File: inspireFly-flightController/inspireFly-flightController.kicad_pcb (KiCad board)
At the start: 2 copper layers, 87 x 80 mm, 23 parts, among them J1 FTSH-107-01-L-DV-K-A, SW1 SW_Push, SW3 SW_Push, U1 STM32U595VITx, Y1 ABS07-32.768KHZ-T

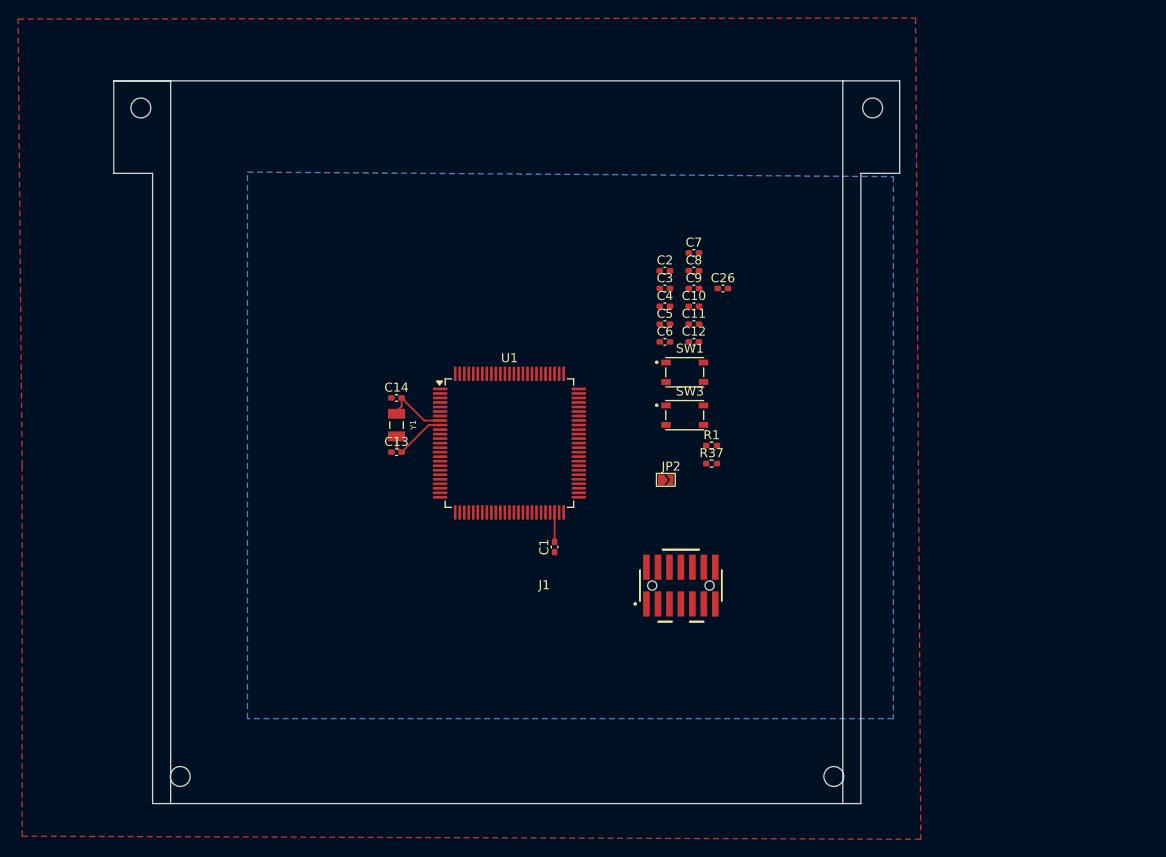
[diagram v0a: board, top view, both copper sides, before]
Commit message: Board sizes + Layer stackup
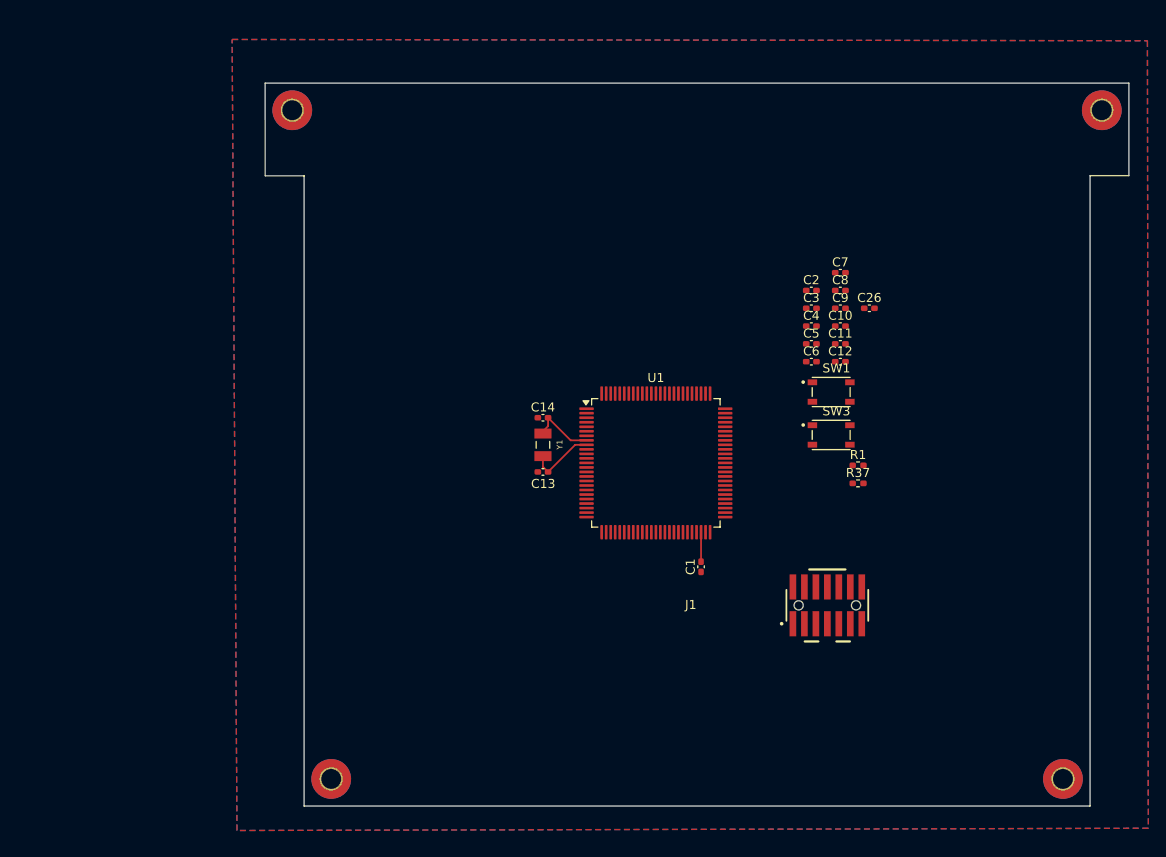
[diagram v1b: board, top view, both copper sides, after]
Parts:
- removed JP2: GND_DETECT, inspirefly:SmallJumper
- added H1: MountingHole_Pad, MountingHole:MountingHole_2.2mm_M2_Pad_TopBottom, F.Cu at (83.5, 42.1)
- added H2: MountingHole_Pad, MountingHole:MountingHole_2.2mm_M2_Pad_TopBottom, F.Cu at (173.1, 42.1)
- added H3: MountingHole_Pad, MountingHole:MountingHole_2.2mm_M2_Pad_TopBottom, F.Cu at (87.8, 116.2)
- added H4: MountingHole_Pad, MountingHole:MountingHole_2.2mm_M2_Pad_TopBottom, F.Cu at (168.8, 116.2)
- U1: value STM32U595VITx -> STM32U595VJT6
- moved C1 16.4 mm to (128.7, 92.7)
- moved C26 16.4 mm to (147.3, 64.1)
- moved R1 16.4 mm to (146.1, 81.5)
- moved R37 16.4 mm to (146.1, 83.5)
- moved SW1 16.4 mm to (143.1, 73.3)
- moved SW3 16.4 mm to (143.1, 78.1)
- moved C10 16.4 mm to (144.1, 66.0)
- moved C3 16.4 mm to (140.9, 64.1)
- moved C4 16.4 mm to (140.9, 66.0)
- moved C9 16.4 mm to (144.1, 64.1)
- moved C11 16.4 mm to (144.1, 68.0)
- moved C12 16.4 mm to (144.1, 70.0)
- moved C13 16.4 mm to (111.2, 82.2)
- moved C14 16.4 mm to (111.2, 76.2)
- moved C2 16.4 mm to (140.9, 62.1)
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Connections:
- J1 pad 11: Net-(JP2-B) -> GND
- U1 pad 15: unconnected-(U1-PC0-Pad15) -> DEBUG_LPUART_RX
- U1 pad 16: unconnected-(U1-PC1-Pad16) -> DEBUG_LPUART_TX
- U1 pad 47: DEBUG_LPUART_RX -> unconnected-(U1-PB10-Pad47)
- U1 pad 51: DEBUG_LPUART_TX -> unconnected-(U1-PB12-Pad51)
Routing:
- added copper zone on In2.Cu, net +3.3V
- added copper zone on In1.Cu, net GND
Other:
- board size 87 x 80 mm -> 95.6 x 80 mm
- copper layers 2 -> 4

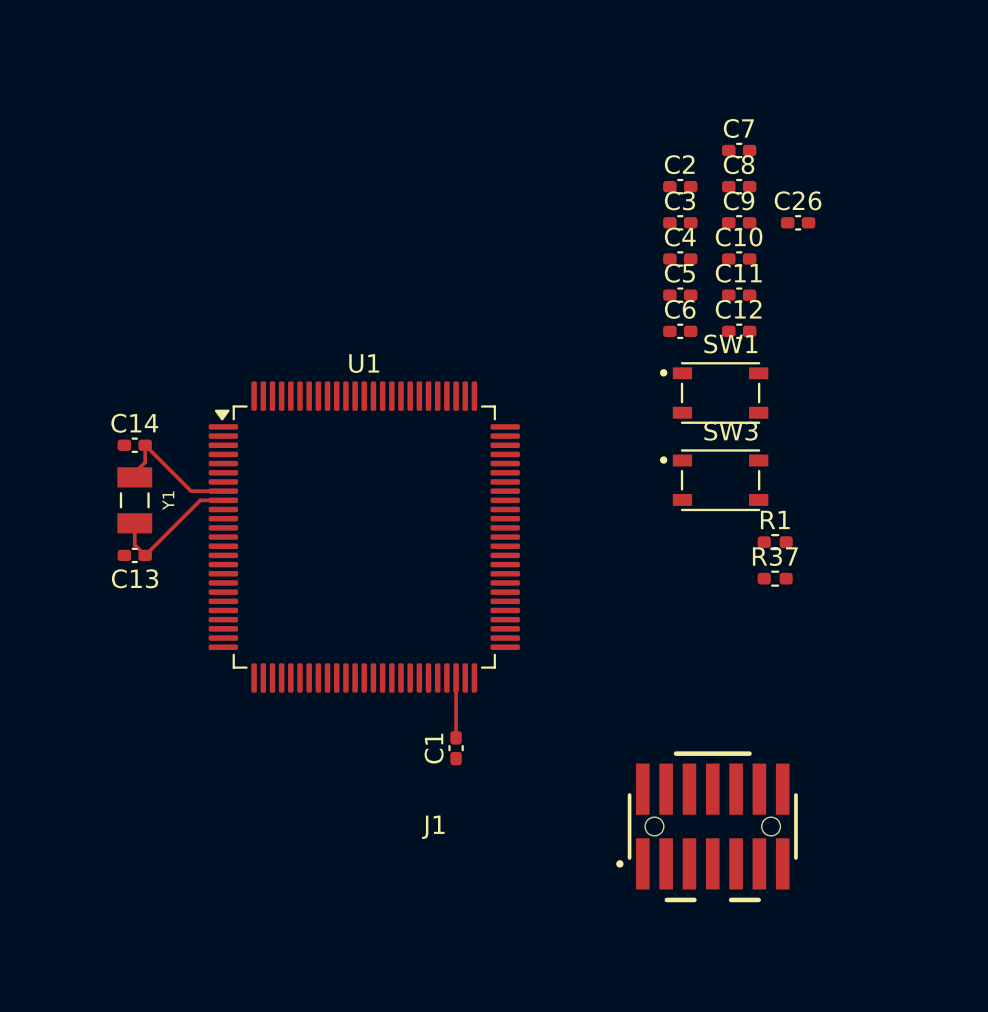
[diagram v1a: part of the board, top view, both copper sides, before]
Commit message: continued routing caps + updated footprints
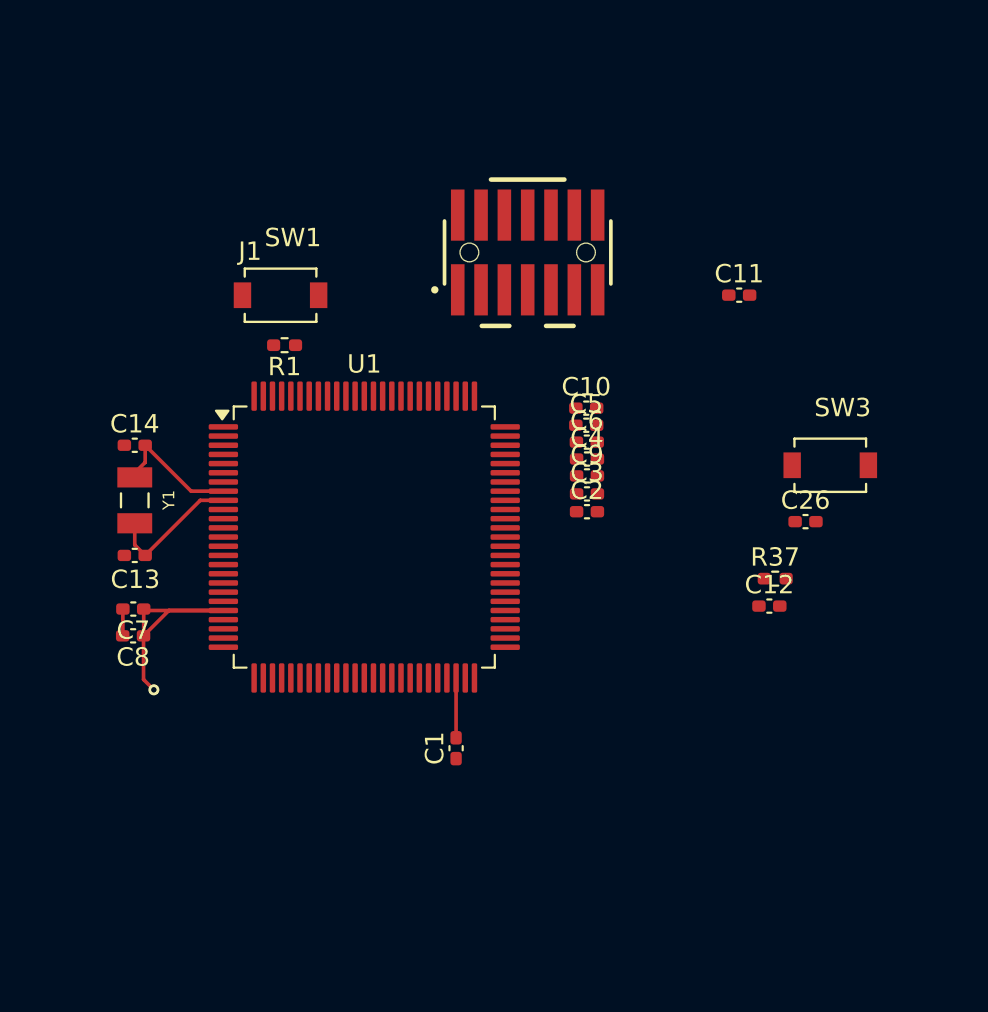
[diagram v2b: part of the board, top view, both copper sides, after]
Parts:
- SW1, SW3: footprint inspireFly-EPS-footprints:SW_PTS810_SJM_250_SMTR_LFS -> inspirefly:SW_TL1015AF160QG
- moved C7 41.4 mm to (111.1, 85.1), turned to 180 degrees
- moved C8 41.1 mm to (111.1, 86.6), turned to 180 degrees
- moved J1 32.8 mm to (132.6, 65.7)
- moved R1 28.8 mm to (119.4, 70.7), turned to 180 degrees
- moved SW1 24.5 mm to (119.2, 68.0)
- moved C2 18.4 mm to (135.8, 79.8)
- moved C26 16.3 mm to (147.7, 80.3)
- moved C9 16.1 mm to (135.8, 77.9)
- moved C3 15.6 mm to (135.8, 78.8)
- moved C12 15.1 mm to (145.8, 85.0)
- moved C4 12.0 mm to (135.8, 76.9)
- moved C10 11.6 mm to (135.8, 74.2)
- moved C5 8.74 mm to (135.8, 75.1)
- moved C6 7.89 mm to (135.8, 76.0)
- moved SW3 6.03 mm to (149.1, 77.3)
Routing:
- net +3.3V: track 0.00 -> 13.9 mm, vias 0 -> 1
- net GND: track 0.00 -> 1.46 mm

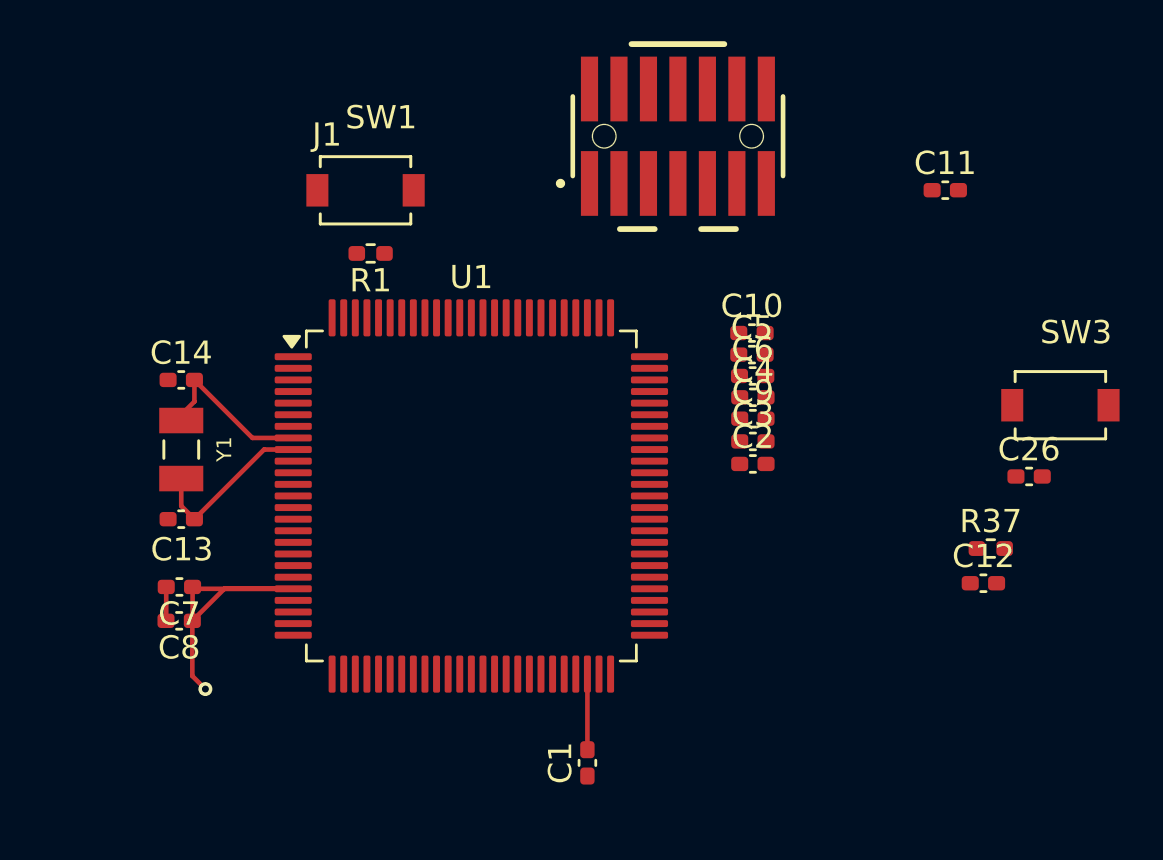
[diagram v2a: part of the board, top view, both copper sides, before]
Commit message: routed all power cap
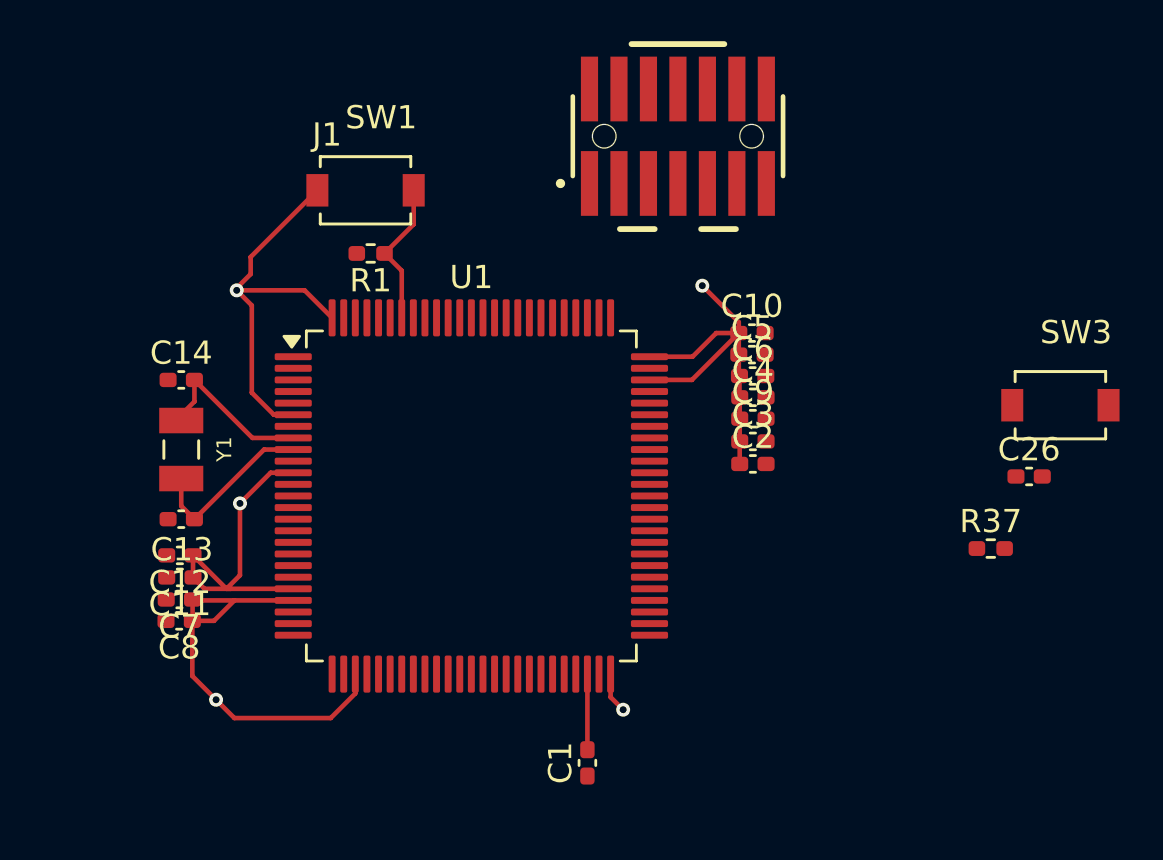
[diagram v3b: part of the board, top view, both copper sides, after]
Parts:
- moved C11 37.0 mm to (111.2, 84.7), turned to 180 degrees
- moved C12 34.6 mm to (111.2, 83.8), turned to 180 degrees
- moved C7 0.54 mm to (111.1, 85.7)
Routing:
- net +3.3V: track 13.9 -> 69.6 mm, vias 1 -> 5
- net Net-(U1-PH3-BOOT0): track 0.00 -> 6.32 mm
- net GND: track 1.46 -> 0.01 mm

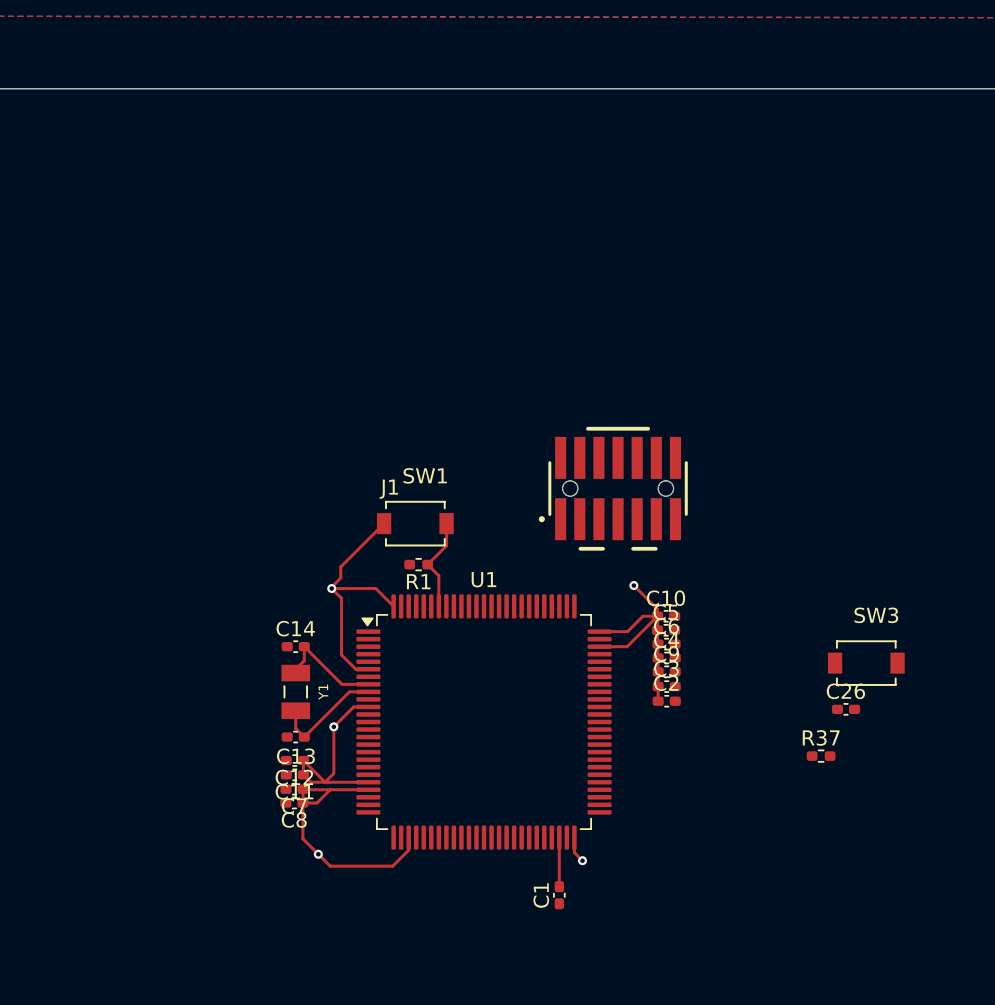
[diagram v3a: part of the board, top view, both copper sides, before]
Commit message: rerouted power caps +stlink
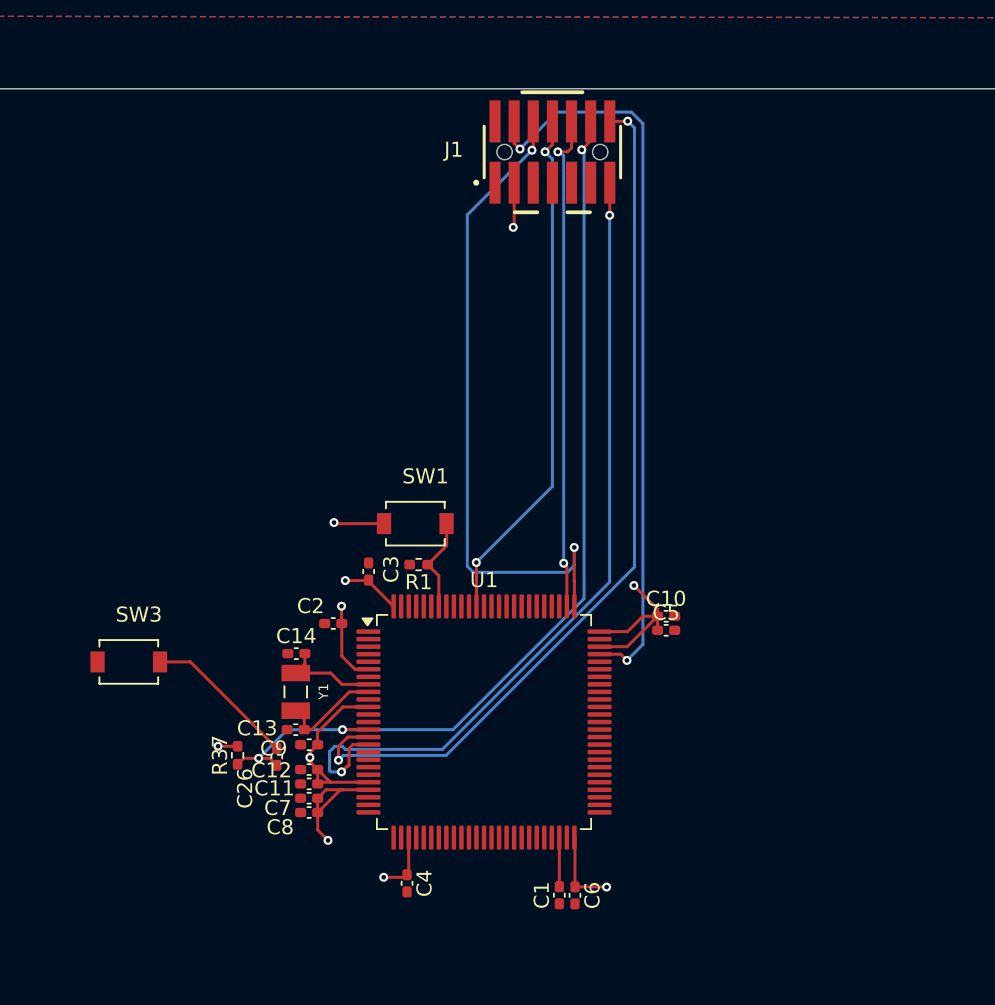
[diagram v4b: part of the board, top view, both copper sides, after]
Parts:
- moved SW3 49.0 mm to (100.1, 77.2)
- moved R37 38.7 mm to (107.3, 83.4), turned to 90 degrees
- moved C26 37.9 mm to (110.0, 83.5), turned to -90 degrees
- moved C9 24.2 mm to (112.1, 82.7), turned to 180 degrees
- moved C4 22.8 mm to (118.6, 91.9), turned to -90 degrees
- moved J1 22.8 mm to (128.2, 43.4)
- moved C2 22.7 mm to (113.7, 74.7), turned to 180 degrees
- moved C3 21.2 mm to (116.0, 71.2), turned to 90 degrees
- moved C6 17.8 mm to (129.8, 92.7), turned to -90 degrees
- moved C8 1.17 mm to (112.1, 87.2)
- moved C7 1.14 mm to (112.1, 86.2)
- moved C11 1.12 mm to (112.1, 85.3)
- moved C12 1.12 mm to (112.1, 84.3)
- moved C13 0.49 mm to (111.2, 81.7)
- moved C14 0.46 mm to (111.2, 76.7)
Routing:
- net NRST: track 0.00 -> 62.7 mm, vias 0 -> 3
- net DEBUG_LPUART_RX: track 0.00 -> 59.1 mm, vias 0 -> 2
- net DEBUG_LPUART_TX: track 0.00 -> 55.2 mm, vias 0 -> 2
- net JTMS/SWDIO: track 0.00 -> 49.5 mm, vias 0 -> 2
- net JTCK/SWCLK: track 0.00 -> 44.0 mm, vias 0 -> 2
- net SWO: track 0.00 -> 34.7 mm, vias 0 -> 2
- net JTDI: track 0.00 -> 33.3 mm, vias 0 -> 2
- net Net-(C26-Pad1): track 0.00 -> 10.1 mm
- net +3.3V: track 69.6 -> 61.8 mm, vias 5 -> 10
- net Net-(U1-PC15-OSC32_OUT): track 7.49 -> 6.79 mm

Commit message: schematic + routing for imu
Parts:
- added C15: 100nF, Capacitor_SMD:C_0402_1005Metric_Pad0.74x0.62mm_HandSolder, F.Cu at (98.5, 94.3)
- added C16: 100nF, Capacitor_SMD:C_0402_1005Metric_Pad0.74x0.62mm_HandSolder, F.Cu at (95.2, 90.7)
- added C22: 100nF, Capacitor_SMD:C_0402_1005Metric_Pad0.74x0.62mm_HandSolder, F.Cu at (97.1, 87.3)
- added R10: 10k, Resistor_SMD:R_0402_1005Metric, F.Cu at (95.2, 91.8)
- added U2: BNO086, inspirefly:BNO086, F.Cu at (100.2, 90.9)
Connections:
- U1 pad 29: unconnected-(U1-PA4-Pad29) -> IMU_SP1_NSS
- U1 pad 30: unconnected-(U1-PA5-Pad30) -> IMU_MCU_SPI1_SCK
- U1 pad 31: unconnected-(U1-PA6-Pad31) -> IMU_MCU_SPI1_MISO
- U1 pad 32: unconnected-(U1-PA7-Pad32) -> H_MDSI_SPI1_MOSI
- U1 pad 39: unconnected-(U1-PE8-Pad39) -> IMU_PSO/WAKE_GPIO
- U1 pad 45: unconnected-(U1-PE14-Pad45) -> IMU_NRST
- U1 pad 46: unconnected-(U1-PE15-Pad46) -> IMU_PSO/WAKE_GPIO
- U1 pad 7: unconnected-(U1-PC13-Pad7) -> IMU_H_INTN_GPIO
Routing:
- net IMU_PSO/WAKE_GPIO: track 0.00 -> 41.9 mm, vias 0 -> 2
- net IMU_NRST: track 0.00 -> 31.8 mm, vias 0 -> 2
- net IMU_H_INTN_GPIO: track 0.00 -> 27.0 mm, vias 0 -> 2
- net H_MDSI_SPI1_MOSI: track 0.00 -> 23.9 mm, vias 0 -> 2
- net IMU_SP1_NSS: track 0.00 -> 22.3 mm, vias 0 -> 2
- net IMU_MCU_SPI1_SCK: track 0.00 -> 21.6 mm, vias 0 -> 2
- net IMU_MCU_SPI1_MISO: track 0.00 -> 19.9 mm, vias 0 -> 2
- net +3.3V: track 61.8 -> 75.3 mm, vias 10 -> 12
- net IMU_BOOTN: track 0.00 -> 2.57 mm
- net Net-(U2-CAP): track 0.00 -> 2.04 mm
